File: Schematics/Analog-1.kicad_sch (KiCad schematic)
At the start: 66 parts, among them J13 Conn_01x03, J14 Conn_01x06, J15 Conn_01x06, U37 MCP4728, U38 MCP4728, U39 MCP4728, U40 MCP4728, U41 MCP4728, U42 MCP4728, U43 MCP4728, U44 MCP4728, U45 MCP4728, U46 TCA9548A, U47 MCP4728, U48 MCP4728, U49 MCP4728, U50 TCA9548A, U51 TCA9548A, U52 MCP4728, U53 MCP4728, U54 MCP4728, U55 MCP4728, U56 MCP4728, U57 MCP4728, U58 LM1117-3.3, U59 MCP4728, U60 MCP4728, U61 MCP4728, U62 MCP4728

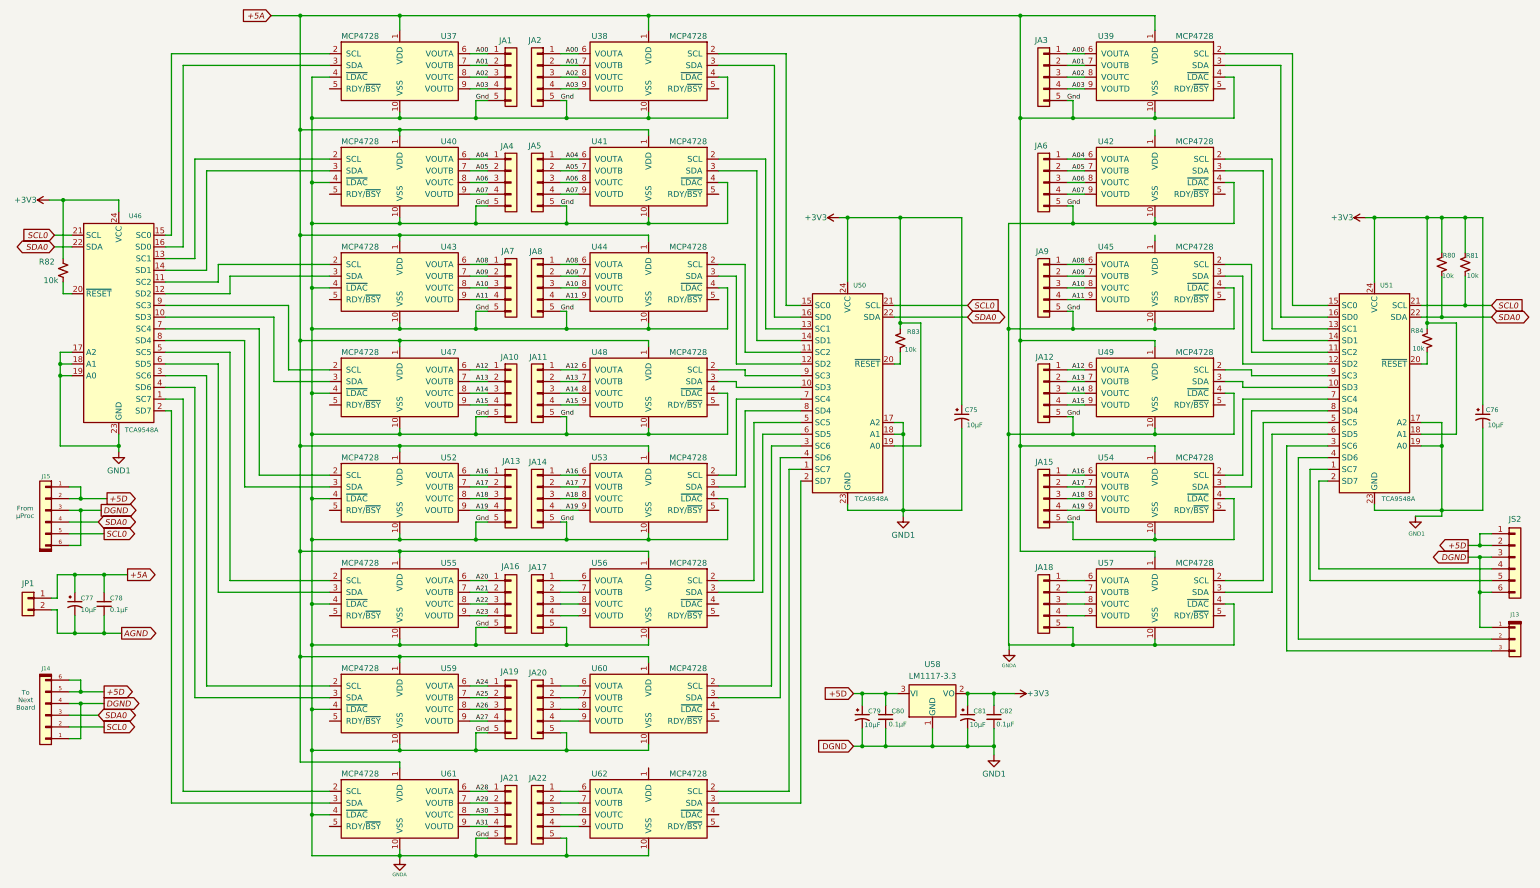
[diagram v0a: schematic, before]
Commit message: Upgreade byte value interface to short.  First stage of refactoring midi input for rotory encoders.  Still needs scaling.
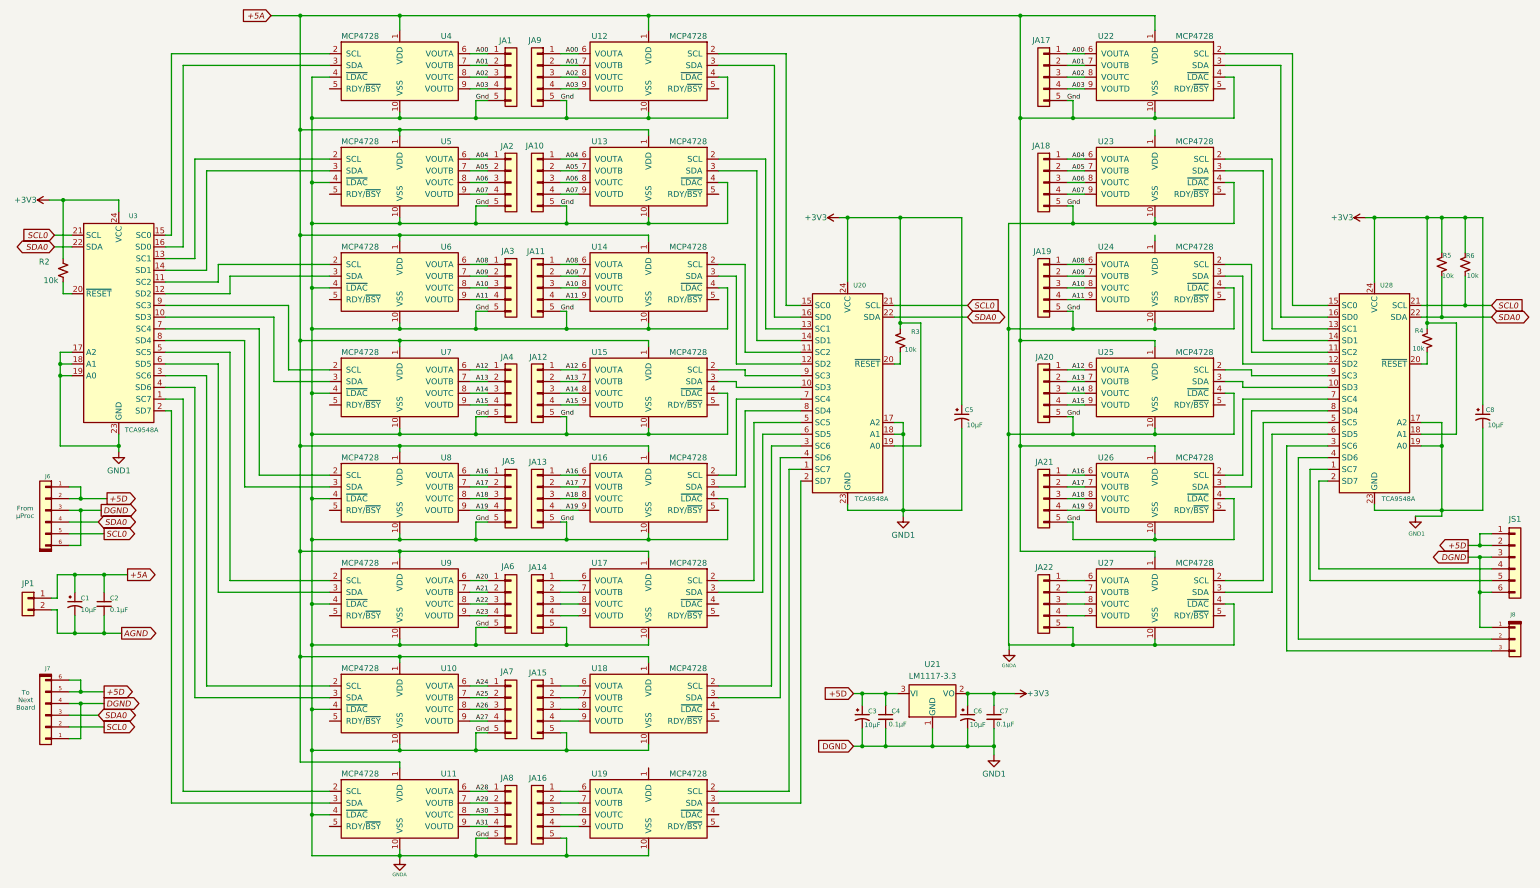
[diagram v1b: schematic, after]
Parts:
- renumbered C77 to C1, C78 to C2, C79 to C3, C80 to C4, C75 to C5, C81 to C6, C82 to C7, C76 to C8, J15 to J6, J14 to J7, J13 to J8, JA5 to JA10, JA8 to JA11, JA11 to JA12, JA14 to JA13, JA17 to JA14, JA20 to JA15, JA22 to JA16, JA3 to JA17, JA6 to JA18, JA9 to JA19, JA4 to JA2, JA12 to JA20, JA15 to JA21, JA18 to JA22, JA7 to JA3, JA10 to JA4, JA13 to JA5, JA16 to JA6, JA19 to JA7, JA21 to JA8, JA2 to JA9, JS2 to JS1, R82 to R2, R83 to R3, R84 to R4, R80 to R5, R81 to R6, U59 to U10, U61 to U11, U38 to U12, U41 to U13, U44 to U14, U48 to U15, U53 to U16, U56 to U17, U60 to U18, U62 to U19, U50 to U20, U58 to U21, U39 to U22, U42 to U23, U45 to U24, U49 to U25, U54 to U26, U57 to U27, U51 to U28, U46 to U3, U37 to U4, U40 to U5, U43 to U6, U47 to U7, U52 to U8, U55 to U9

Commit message: Updated schematics including VCO and VCF daughter boards
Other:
- company:       MLE Tech                  Cedar Park, TX -> (none)
- title: Synth #2 -> Digital to Analog
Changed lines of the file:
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@@
 	(paper "USLegal")
 	(title_block
-		(title "Synth #2")
-		(date "2023-07-27")
-		(rev "0.1")
-		(company "      MLE Tech                  Cedar Park, TX")
-		(comment 2 "In Development")
+		(title "Digital to Analog")
+		(date "2025-01-16")
+		(rev "2.2")
+		(comment 1 "In Development ")
 	)
 	(junction

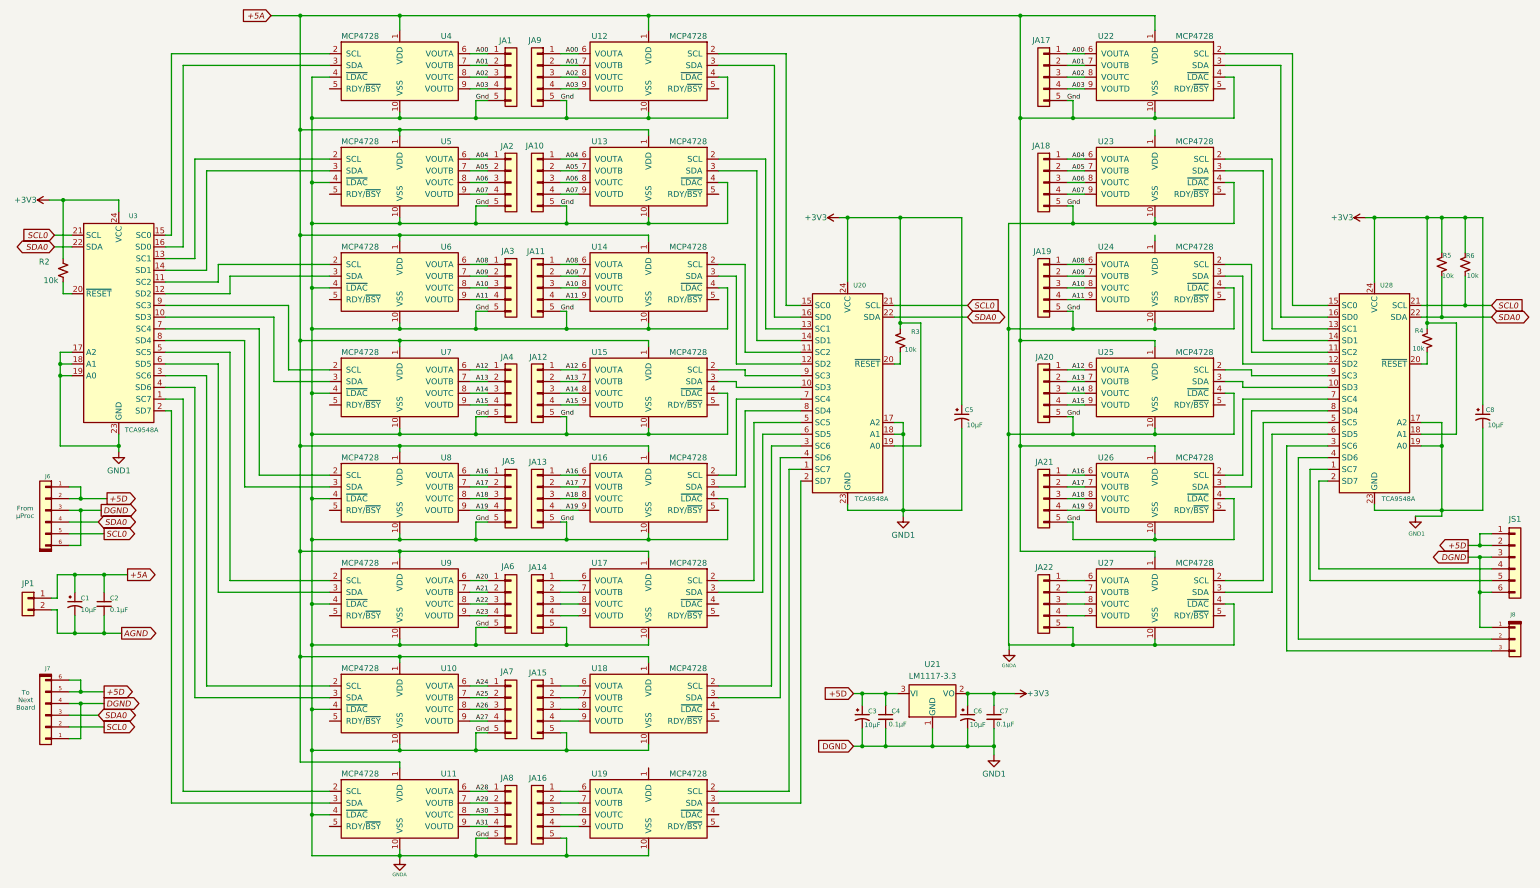
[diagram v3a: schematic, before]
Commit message: Fixed bugs in voice selection on configuration.  Reorganized schematics to have different master drawings for power and audio paths.  Started work on dual 3-pole state variable filter with resonance.
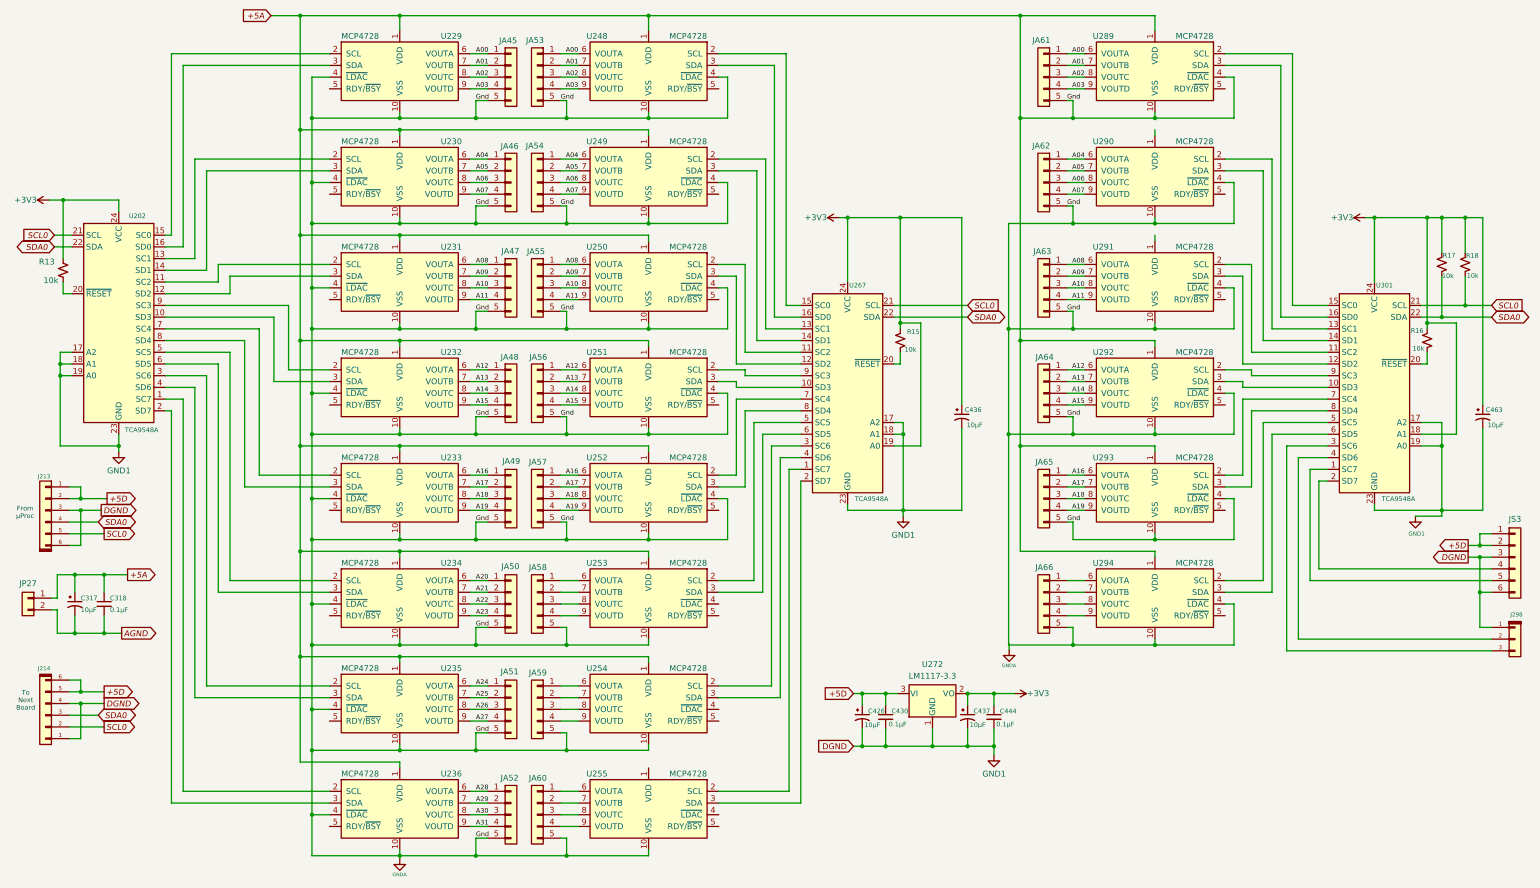
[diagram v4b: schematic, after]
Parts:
- renumbered C1 to C317, C2 to C318, C3 to C426, C4 to C430, C5 to C436, C6 to C437, C7 to C444, C8 to C463, J6 to J213, J7 to J214, J8 to J298, JA1 to JA45, JA2 to JA46, JA3 to JA47, JA4 to JA48, JA5 to JA49, JA6 to JA50, JA7 to JA51, JA8 to JA52, JA9 to JA53, JA10 to JA54, JA11 to JA55, JA12 to JA56, JA13 to JA57, JA14 to JA58, JA15 to JA59, JA16 to JA60, JA17 to JA61, JA18 to JA62, JA19 to JA63, JA20 to JA64, JA21 to JA65, JA22 to JA66, JP1 to JP27, JS1 to JS3, R2 to R13, R3 to R15, R4 to R16, R5 to R17, R6 to R18, U3 to U202, U4 to U229, U5 to U230, U6 to U231, U7 to U232, U8 to U233, U9 to U234, U10 to U235, U11 to U236, U12 to U248, U13 to U249, U14 to U250, U15 to U251, U16 to U252, U17 to U253, U18 to U254, U19 to U255, U20 to U267, U21 to U272, U22 to U289, U23 to U290, U24 to U291, U25 to U292, U26 to U293, U27 to U294, U28 to U301

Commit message: Refactored hardware and software.  Improved Launch Control XL configuration and control.
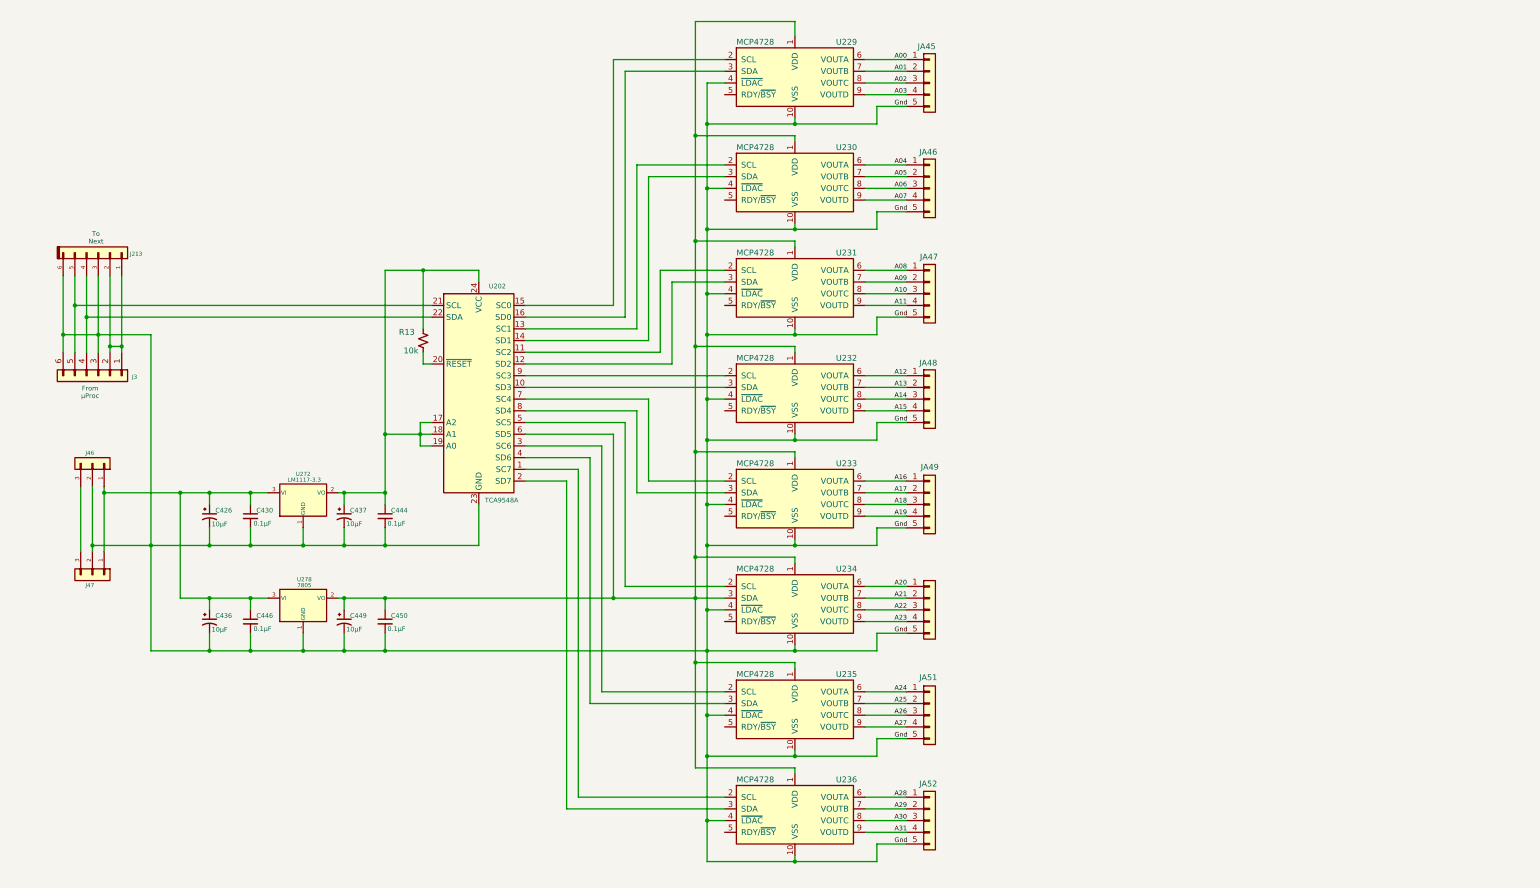
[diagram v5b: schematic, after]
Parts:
- removed C317, C463: 10µF, symbol Device:C_Polarized_Small_US
- removed C318: 0.1µF, symbol Device:C_Small
- removed J214: Conn_01x06, symbol My Connectors:Conn_01x06
- removed J298: Conn_01x03, symbol My Connectors:Conn_01x03
- removed JA53, JA61: DA00, symbol Connector_Generic:Conn_01x05
- removed JA54, JA62: DA04, symbol Connector_Generic:Conn_01x05
- removed JA55, JA63: DA08, symbol Connector_Generic:Conn_01x05
- removed JA56, JA64: DA12, symbol Connector_Generic:Conn_01x05
- removed JA57, JA58, JA59, JA60, JA65, JA66: DA16, symbol Connector_Generic:Conn_01x05
- removed JP27: From 12v Analog, symbol Connector_Generic:Conn_01x02
- removed R15, R16, R17, R18: 10k, symbol Device:R_Small_US
- removed U248, U249, U250, U251, U252, U253, U254, U255, U289, U290, U291, U292, U293, U294: MCP4728, Package_SO:MSOP-10_3x3mm_P0.5mm, symbol Analog_DAC:MCP4728
- removed U267, U301: TCA9548A, Package_SO:SOIC-24W_7.5x15.4mm_P1.27mm, symbol Interface_Expansion:PCA9548ADW
- added C446, C450: 0.1µF, symbol Device:C_Small
- added C449: 10µF, symbol Device:C_Polarized_Small_US
- added J46, J47: Conn_01x03, symbol Connector_Generic:Conn_01x03
- added U278: 7805, symbol Regulator_Linear:LM1117-3.3
- renumbered JS3 to J3
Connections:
- net SCL0 is gone; now on an unnamed net: J213.5 (Pin_5), U202.21 (SCL)
- net SDA0 is gone; now on an unnamed net: J213.4 (Pin_4), U202.22 (SDA)
- net at U202.6 (SD5), U234.3 (SDA): now also U229.1 (VDD), U230.1 (VDD), U231.1 (VDD), U232.1 (VDD), U233.1 (VDD), U234.1 (VDD), U235.1 (VDD), U236.1 (VDD), C449.1, C450.1, U278.2 (VO)
- net +3V3: no longer names the net of C437.1, C444.1, U272.2 (VO)
- net +3V3: now also U202.17 (A2), U202.18 (A1), U202.19 (A0); no longer C436.1, R13.1, U202.24 (VCC)
- net +5D: no longer names the net of J213.1 (Pin_1), J213.2 (Pin_2), J3.1 (Pin_1), J3.2 (Pin_2)
- net +5D: no longer C426.1, C430.1, U272.3 (VI)
- net GND1 renamed Gnd
- net Gnd: now also JA45.5 (Pin_5), JA46.5 (Pin_5), JA47.5 (Pin_5), JA48.5 (Pin_5), JA49.5 (Pin_5), JA50.5 (Pin_5), JA51.5 (Pin_5), JA52.5 (Pin_5), U229.10 (VSS), U229.4 (~{LDAC}), U230.10 (VSS), U230.4 (~{LDAC}), U231.10 (VSS), U231.4 (~{LDAC}), U232.10 (VSS), U232.4 (~{LDAC}), U233.10 (VSS), U233.4 (~{LDAC}), U234.10 (VSS), U234.4 (~{LDAC}), U235.10 (VSS), U235.4 (~{LDAC}), U236.10 (VSS), U236.4 (~{LDAC}), C446.2, C449.2, C450.2, J46.2 (Pin_2), J47.2 (Pin_2), U278.1 (GND); no longer U202.17 (A2), U202.18 (A1), U202.19 (A0)
- removed net GNDA: JA45.5 (Pin_5), JA46.5 (Pin_5), JA47.5 (Pin_5), JA48.5 (Pin_5), JA49.5 (Pin_5), JA50.5 (Pin_5), JA51.5 (Pin_5), JA52.5 (Pin_5), U229.1 (VDD), U229.10 (VSS), U229.4 (~{LDAC}), U230.1 (VDD), U230.10 (VSS), U230.4 (~{LDAC}), U231.1 (VDD), U231.10 (VSS), U231.4 (~{LDAC}), U232.1 (VDD), U232.10 (VSS), U232.4 (~{LDAC}), U233.1 (VDD), U233.10 (VSS), U233.4 (~{LDAC}), U234.1 (VDD), U234.10 (VSS), U234.4 (~{LDAC}), U235.1 (VDD), U235.10 (VSS), U235.4 (~{LDAC}), U236.1 (VDD), U236.10 (VSS), U236.4 (~{LDAC})
- new net: R13.1, U202.24 (VCC)
- new net: C426.1, C430.1, C436.1, C446.1, J46.1 (Pin_1), J47.1 (Pin_1), U272.3 (VI), U278.3 (VI)
- new net: J46.3 (Pin_3), J47.3 (Pin_3)
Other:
- note added: "To Next"
- note removed: "To Next Board"
- moved on the sheet: C426, C430, C437, C444, J213, J3, JA45, JA46, JA47, JA48, JA49, JA51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
